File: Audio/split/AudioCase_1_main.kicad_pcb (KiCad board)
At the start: 2 copper layers, 162.9 x 98.2 mm, 40 parts, among them J12 AMP1_PWR, J13 ROTARY_SW, J14 AMP_PWR_IN, J15 PD_IN, J16 AUDIO_IN, J17 OLED_PIN, J18 AMP1_LR, J19 AMP2_PWR, J20 AMP2_LR, J21 AMP3_PWR, J22 AMP4_PWR, J23 AMP5_PWR, J24 AMP3_LR, J25 AMP4_LR, J26 AMP5_LR, K1 AZ850P2-x, K10 AZ850P2-x, K2 AZ850P2-x, K3 AZ850P2-x, K4 AZ850P2-x, K5 AZ850P2-x, K6 AZ850P2-x, K7 AZ850P2-x, K8 AZ850P2-x, K9 AZ850P2-x, U4 BP5293-50, U5 ULN2803A, U6 ULN2803A, U7 ULN2803A

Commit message: ノイズ対策と製造データ整備: デカップリング追加・GNDベタ強化・シルク整理
- 5V_+ラインにデカップリング/バルク(C34-C37)を追加し、リレー切替時の電源変動を抑制
- F.CuにCTRL_GND/GNDベタを追加し、ステッチングビアで表裏GNDを補強(DC-DC周辺含む)
- 端子台ラベル等のシルク重なりを解消(J11/J14/J6/J4/L1/L2ほか)
- masterから4基板を再split、Gerber/zipを再生成

Co-authored-by: Cursor <cursoragent@cursor.com>
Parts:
- added C34: 0.1μF, Capacitor_SMD:C_1206_3216Metric_Pad1.33x1.80mm_HandSolder, B.Cu at (172.7, 107.5)
- added C35: 0.1μF, Capacitor_SMD:C_1206_3216Metric_Pad1.33x1.80mm_HandSolder, B.Cu at (123.8, 74.4)
- added C36: 0.1μF, Capacitor_SMD:C_1206_3216Metric_Pad1.33x1.80mm_HandSolder, B.Cu at (150.4, 74.5)
- added C37: 0.1μF, Capacitor_SMD:C_1206_3216Metric_Pad1.33x1.80mm_HandSolder, B.Cu at (176.1, 74.8)
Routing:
- net /Controll/5V_+: track 489.2 -> 503.2 mm
- net /Controll/CTRL_GND: vias 3 -> 30
- added copper zone on F.Cu, net /Controll/CTRL_GND
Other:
- board text added: "+"
- board text added: "-"
- board text added: "L"
- board text added: "R"

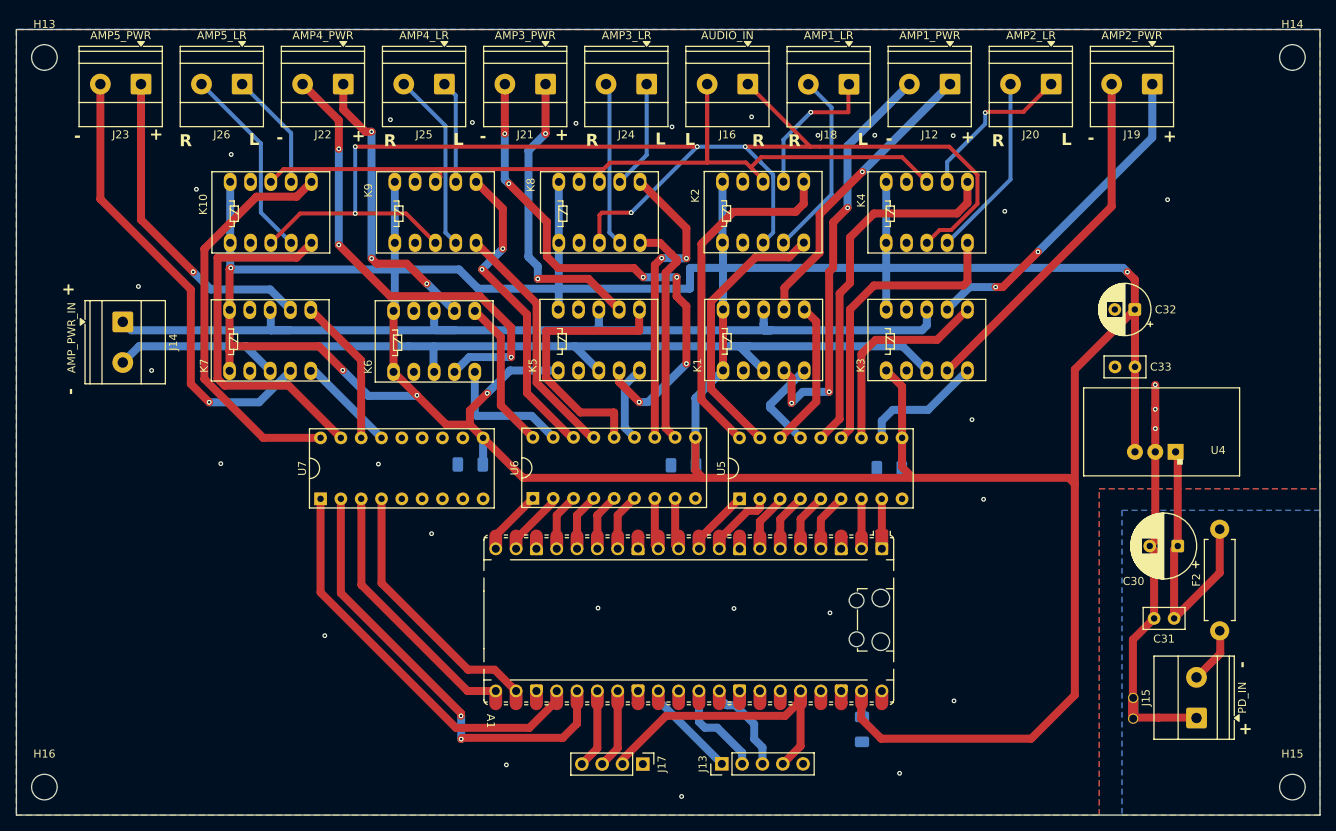
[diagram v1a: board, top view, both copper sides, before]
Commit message: AudioCaseのリレー・EQネット整理と分割Gerberを再生成する。
Controllでアンプ別リレーネットを分離し、EQのバッファ入力をL/R_BUFF_INに改名。4枚分割PCBと発注用Gerberを更新し、RVパネルKiKit矩形とmacOS向けツール探索も修正。

Co-authored-by: Cursor <cursoragent@cursor.com>
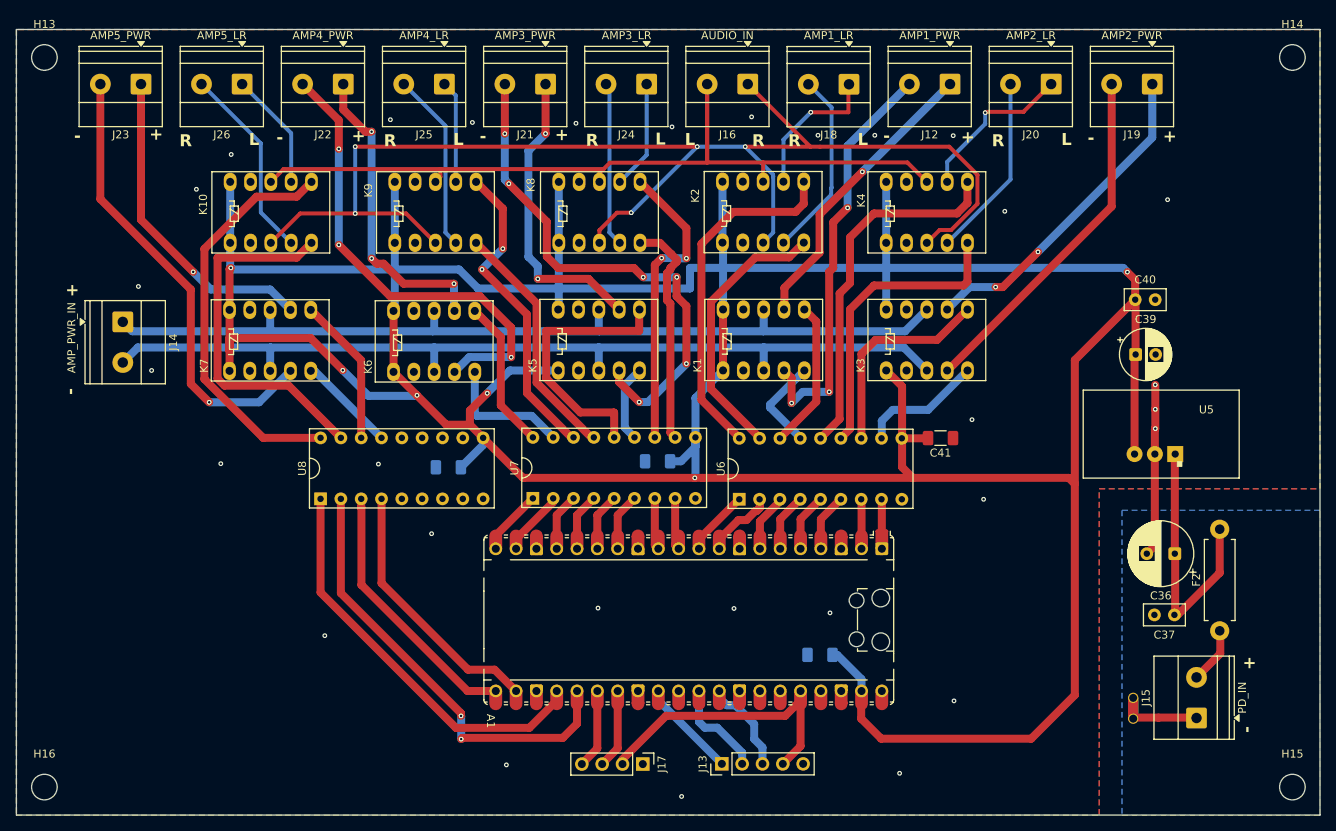
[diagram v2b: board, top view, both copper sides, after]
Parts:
- removed C30: 47μF, Capacitor_THT:CP_Radial_D8.0mm_P3.50mm
- removed C31, C33: 0.1μF, Capacitor_THT:C_Disc_D5.0mm_W2.5mm_P2.50mm
- removed C32: 100μF, Capacitor_THT:CP_Radial_D6.3mm_P2.50mm
- removed C34, C35: 0.1μF, Capacitor_SMD:C_1206_3216Metric_Pad1.33x1.80mm_HandSolder
- removed U4: BP5293-50, BP5293_ROHM:BP5293-50_ROHM_SIP-3
- added C38: 0.1μF, Capacitor_SMD:C_1206_3216Metric_Pad1.33x1.80mm_HandSolder, B.Cu at (167.5, 98.2)
- added C39: 100μF, Capacitor_THT:CP_Radial_D6.3mm_P2.50mm, F.Cu at (206.9, 60.6)
- added C40: 0.1μF, Capacitor_THT:C_Disc_D5.0mm_W2.5mm_P2.50mm, F.Cu at (206.9, 53.8)
- added C41: 0.1μF, Capacitor_SMD:C_1206_3216Metric_Pad1.33x1.80mm_HandSolder, F.Cu at (182.5, 71.1)
- added C42: 0.1μF, Capacitor_SMD:C_1206_3216Metric_Pad1.33x1.80mm_HandSolder, B.Cu at (147.2, 74.0)
- added C43: 0.1μF, Capacitor_SMD:C_1206_3216Metric_Pad1.33x1.80mm_HandSolder, B.Cu at (121.0, 74.7)
- added U8: ULN2803A, Library:ULN2803A_DIP-18_W7.62mm, F.Cu at (115.2, 74.9)
- C36: value 0.1μF -> 47μF; footprint Capacitor_SMD:C_1206_3216Metric_Pad1.33x1.80mm_HandSolder -> Capacitor_THT:CP_Radial_D8.0mm_P3.50mm; moved to F.Cu
- C37: footprint Capacitor_SMD:C_1206_3216Metric_Pad1.33x1.80mm_HandSolder -> Capacitor_THT:C_Disc_D5.0mm_W2.5mm_P2.50mm; moved to F.Cu
- U5: value ULN2803A -> BP5293-50; footprint Library:ULN2803A_DIP-18_W7.62mm -> BP5293_ROHM:BP5293-50_ROHM_SIP-3
- moved C36 62.4 mm to (211.8, 85.5), turned to 180 degrees
- moved U5 44.3 mm to (211.9, 73.1), turned to 180 degrees
- moved C37 40.1 mm to (211.8, 93.2), turned to 180 degrees
- moved U7 26.5 mm to (141.7, 74.8)
- moved U6 25.8 mm to (167.5, 74.9)
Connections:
- C36 pad 1: /Controll/CTRL_GND -> Net-(U5-VIN)
- C36 pad 2: /Controll/5V_+ -> /Controll/CTRL_GND
- C37 pad 1: /Controll/CTRL_GND -> Net-(U5-VIN)
- C37 pad 2: /Controll/5V_+ -> /Controll/CTRL_GND
- F2 pad 2: Net-(U4-VIN) -> Net-(U5-VIN)
- J12 pad 1: /Controll/AMP_V+_OUT -> /Controll/AMP_1_V+_OUT
- J12 pad 2: /Controll/AMP_V-_OUT -> /Controll/AMP_1_V-_OUT
- J18 pad 1: /Controll/L_OUT -> /Controll/AMP_1_L_OUT
- J18 pad 2: /Controll/R_OUT -> /Controll/AMP_1_R_OUT
- J19 pad 1: /Controll/AMP_V+_OUT -> /Controll/AMP_2_V+_OUT
- J19 pad 2: /Controll/AMP_V-_OUT -> /Controll/AMP_2_V-_OUT
- J20 pad 1: /Controll/L_OUT -> /Controll/AMP_2_L_OUT
- J20 pad 2: /Controll/R_OUT -> /Controll/AMP_2_R_OUT
- J21 pad 1: /Controll/AMP_V+_OUT -> /Controll/AMP_3_V+_OUT
- J21 pad 2: /Controll/AMP_V-_OUT -> /Controll/AMP_3_V-_OUT
- J22 pad 1: /Controll/AMP_V+_OUT -> /Controll/AMP_4_V+_OUT
- J22 pad 2: /Controll/AMP_V-_OUT -> /Controll/AMP_4_V-_OUT
- J23 pad 1: /Controll/AMP_V+_OUT -> /Controll/AMP_5_V+_OUT
- J23 pad 2: /Controll/AMP_V-_OUT -> /Controll/AMP_5_V-_OUT
- J24 pad 1: /Controll/L_OUT -> /Controll/AMP_3_L_OUT
- J24 pad 2: /Controll/R_OUT -> /Controll/AMP_3_R_OUT
- J25 pad 1: /Controll/L_OUT -> /Controll/AMP_4_L_OUT
- J25 pad 2: /Controll/R_OUT -> /Controll/AMP_4_R_OUT
- J26 pad 1: /Controll/L_OUT -> /Controll/AMP_5_L_OUT
- J26 pad 2: /Controll/R_OUT -> /Controll/AMP_5_R_OUT
- K1 pad 4: /Controll/AMP_V-_OUT -> /Controll/AMP_1_V-_OUT
- K1 pad 7: /Controll/AMP_V+_OUT -> /Controll/AMP_1_V+_OUT
- K10 pad 4: /Controll/R_OUT -> /Controll/AMP_5_R_OUT
- K10 pad 7: /Controll/L_OUT -> /Controll/AMP_5_L_OUT
- K2 pad 4: /Controll/R_OUT -> /Controll/AMP_1_R_OUT
- K2 pad 7: /Controll/L_OUT -> /Controll/AMP_1_L_OUT
- K3 pad 4: /Controll/AMP_V-_OUT -> /Controll/AMP_2_V-_OUT
- K3 pad 7: /Controll/AMP_V+_OUT -> /Controll/AMP_2_V+_OUT
- K4 pad 4: /Controll/R_OUT -> /Controll/AMP_2_R_OUT
- K4 pad 7: /Controll/L_OUT -> /Controll/AMP_2_L_OUT
- K5 pad 4: /Controll/AMP_V-_OUT -> /Controll/AMP_3_V-_OUT
- K5 pad 7: /Controll/AMP_V+_OUT -> /Controll/AMP_3_V+_OUT
- K6 pad 4: /Controll/AMP_V-_OUT -> /Controll/AMP_4_V-_OUT
- K6 pad 7: /Controll/AMP_V+_OUT -> /Controll/AMP_4_V+_OUT
- K7 pad 4: /Controll/AMP_V-_OUT -> /Controll/AMP_5_V-_OUT
- K7 pad 7: /Controll/AMP_V+_OUT -> /Controll/AMP_5_V+_OUT
- K8 pad 4: /Controll/R_OUT -> /Controll/AMP_3_R_OUT
- K8 pad 7: /Controll/L_OUT -> /Controll/AMP_3_L_OUT
- K9 pad 4: /Controll/R_OUT -> /Controll/AMP_4_R_OUT
- K9 pad 7: /Controll/L_OUT -> /Controll/AMP_4_L_OUT
- U5 pad 1: /Controll/PWR_RESET_GPIO_2 -> Net-(U5-VIN)
- U5 pad 2: /Controll/PWR_SET_GPIO_2 -> /Controll/CTRL_GND
- U5 pad 3: /Controll/AUDIO_RESET_GPIO_2 -> /Controll/5V_+
- U6 pad 1: /Controll/PWR_RESET_GPIO_4 -> /Controll/PWR_RESET_GPIO_2
- U6 pad 11: /Controll/AUDIO_SET_RELAY_3 -> /Controll/PWR_SET_RELAY_2
- U6 pad 12: /Controll/AUDIO_RESET_RELAY_3 -> /Controll/PWR_RESET_RELAY_2
- U6 pad 13: /Controll/PWR_SET_RELAY_3 -> /Controll/AUDIO_SET_RELAY_2
- U6 pad 14: /Controll/PWR_RESET_RELAY_3 -> /Controll/AUDIO_RESET_RELAY_2
- U6 pad 15: /Controll/AUDIO_SET_RELAY_4 -> /Controll/PWR_SET_RELAY_1
- U6 pad 16: /Controll/AUDIO_RESET_RELAY_4 -> /Controll/PWR_RESET_RELAY_1
- U6 pad 17: /Controll/PWR_SET_RELAY_4 -> /Controll/AUDIO_SET_RELAY_1
- U6 pad 18: /Controll/PWR_RESET_RELAY_4 -> /Controll/AUDIO_RESET_RELAY_1
- U6 pad 2: /Controll/PWR_SET_GPIO_4 -> /Controll/PWR_SET_GPIO_2
- U6 pad 3: /Controll/AUDIO_RESET_GPIO_4 -> /Controll/AUDIO_RESET_GPIO_2
- U6 pad 4: /Controll/AUDIO_SET_GPIO_4 -> /Controll/AUDIO_SET_GPIO_2
- U6 pad 5: /Controll/PWR_RESET_GPIO_3 -> /Controll/PWR_RESET_GPIO_1
- U6 pad 6: /Controll/PWR_SET_GPIO_3 -> /Controll/PWR_SET_GPIO_1
- U6 pad 7: /Controll/AUDIO_RESET_GPIO_3 -> /Controll/AUDIO_RESET_GPIO_1
- U6 pad 8: /Controll/AUDIO_SET_GPIO_3 -> /Controll/AUDIO_SET_GPIO_1
- U7 pad 1: /Controll/AUDIO_RESET_GPIO_5 -> /Controll/PWR_RESET_GPIO_4
- U7 pad 11: unconnected-(U7-O8-Pad11) -> /Controll/AUDIO_SET_RELAY_3
- U7 pad 12: unconnected-(U7-O7-Pad12) -> /Controll/AUDIO_RESET_RELAY_3
- U7 pad 13: unconnected-(U7-O6-Pad13) -> /Controll/PWR_SET_RELAY_3
- U7 pad 14: unconnected-(U7-O5-Pad14) -> /Controll/PWR_RESET_RELAY_3
- U7 pad 15: /Controll/PWR_SET_RELAY_5 -> /Controll/AUDIO_SET_RELAY_4
- U7 pad 16: /Controll/PWR_RESET_RELAY_5 -> /Controll/AUDIO_RESET_RELAY_4
- U7 pad 17: /Controll/AUDIO_SET_RELAY_5 -> /Controll/PWR_SET_RELAY_4
- U7 pad 18: /Controll/AUDIO_RESET_RELAY_5 -> /Controll/PWR_RESET_RELAY_4
- U7 pad 2: /Controll/AUDIO_SET_GPIO_5 -> /Controll/PWR_SET_GPIO_4
- U7 pad 3: /Controll/PWR_RESET_GPIO_5 -> /Controll/AUDIO_RESET_GPIO_4
- U7 pad 4: /Controll/PWR_SET_GPIO_5 -> /Controll/AUDIO_SET_GPIO_4
- U7 pad 5: /Controll/CTRL_GND -> /Controll/PWR_RESET_GPIO_3
- U7 pad 6: /Controll/CTRL_GND -> /Controll/PWR_SET_GPIO_3
- U7 pad 7: /Controll/CTRL_GND -> /Controll/AUDIO_RESET_GPIO_3
- U7 pad 8: /Controll/CTRL_GND -> /Controll/AUDIO_SET_GPIO_3
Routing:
- net /Controll/AMP_V-_OUT: track 278.5 -> 0.00 mm, vias 13 -> 0
- net /Controll/AMP_V+_OUT: track 192.6 -> 0.00 mm, vias 9 -> 0
- net /Controll/R_OUT: track 114.2 -> 0.00 mm
- net /Controll/L_OUT: track 79.9 -> 0.00 mm, vias 2 -> 0
- net /Controll/AMP_3_V-_OUT: track 0.00 -> 65.3 mm, vias 0 -> 6
- net /Controll/AMP_4_V-_OUT: track 0.00 -> 59.3 mm, vias 0 -> 3
- net /Controll/AMP_5_V-_OUT: track 0.00 -> 57.2 mm, vias 0 -> 1
- net /Controll/AMP_1_V-_OUT: track 0.00 -> 52.4 mm, vias 0 -> 3
- net /Controll/AMP_2_V-_OUT: track 0.00 -> 44.4 mm
- net /Controll/AMP_2_V+_OUT: track 0.00 -> 41.2 mm, vias 0 -> 2
- net /Controll/AMP_5_V+_OUT: track 0.00 -> 40.3 mm, vias 0 -> 1
- net /Controll/AMP_4_V+_OUT: track 0.00 -> 38.8 mm, vias 0 -> 3
- net /Controll/AMP_3_V+_OUT: track 0.00 -> 37.5 mm, vias 0 -> 2
- net /Controll/AMP_1_V+_OUT: track 0.00 -> 36.8 mm, vias 0 -> 1
- net Net-(U4-VIN): track 34.6 -> 0.00 mm
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
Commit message: 分割Gerberを再生成し、05のzip名をスクリプト表記に揃える。
初号向け再出力を取り込み、旧05_rv_conv.zipを05_rv_convert.zipへ置き換える。

Co-authored-by: Cursor <cursoragent@cursor.com>
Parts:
- U5: footprint BP5293_ROHM:BP5293-50_ROHM_SIP-3 -> Library:BP5293-50_ROHM_SIP-3
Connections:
- net /Controll/PD_GND_IN renamed /MeasurementADC/ADC_GND_IN
